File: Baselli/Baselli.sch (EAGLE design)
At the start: 45 parts, among them J2 DF12-ELLI-HEADER-TOP, J3 DF12-ELLI-RECEPTABLE-BOTTOM, J4 FTDI-SER-6-PP, J5 JTAG_PROG, Q1 MOSFET-PCHANNELIRLML2244, U1 LCMXO2-256HC-4SG32, U2 STM32F051R

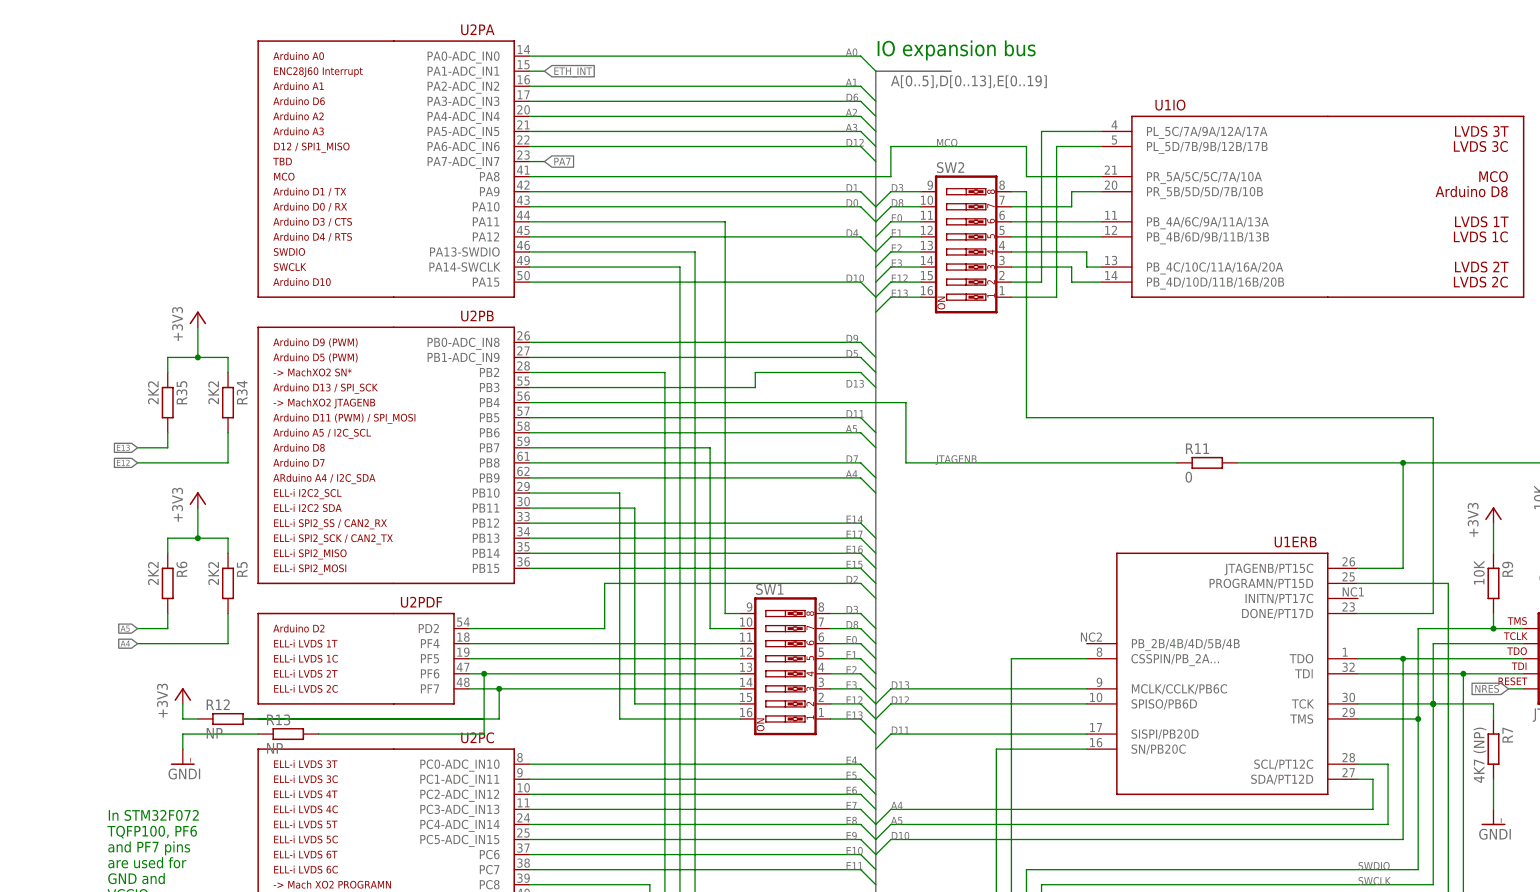
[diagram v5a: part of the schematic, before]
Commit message: Replaced DIP switches with series resistors in Baselli
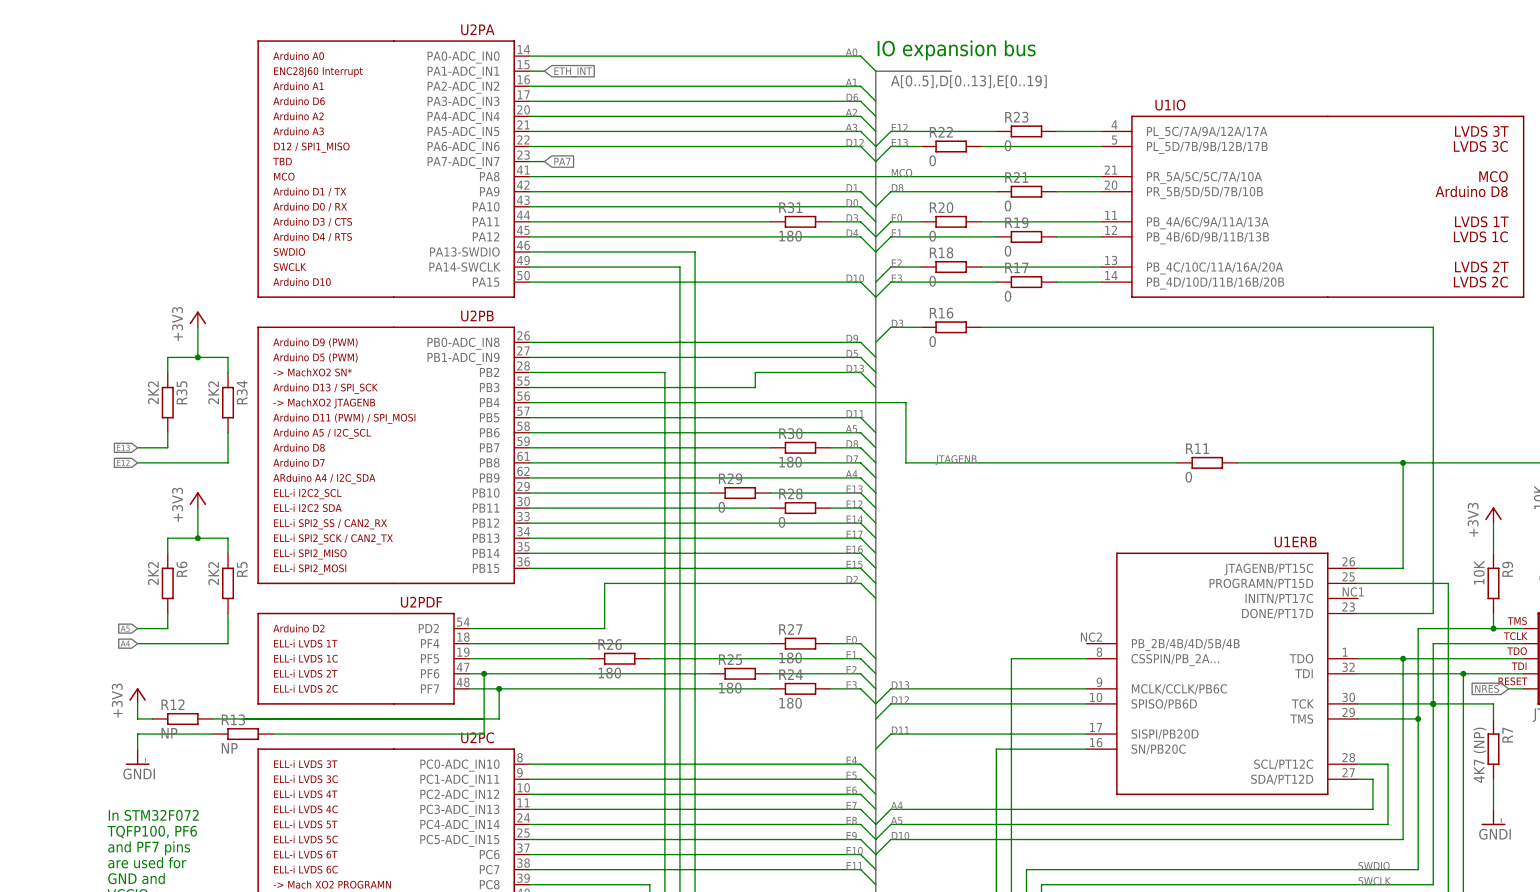
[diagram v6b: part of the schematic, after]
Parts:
- removed SW1, SW2: (no value), SparkFun-Electromechanical:SW_DIP-8-SMT-HALFSIZE
- added R16, R17, R18, R19, R20, R21, R22, R23, R28, R29: 0, ELL-i-Passives:R0805
- added R24, R25, R26, R27, R30, R31: 180, ELL-i-Passives:R0805
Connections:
- net D3: now also R16.1, R31.2; no longer SW1.8, SW2.9
- net D8: now also R21.1, R30.2; no longer SW1.7, SW2.10
- net DONE: now also R16.2; no longer SW2.8
- net E0: now also R20.1, R27.2; no longer SW1.6, SW2.11
- net E1: now also R19.1, R26.2; no longer SW1.5, SW2.12
- net E12: now also R23.1, R28.2; no longer SW1.2, SW2.15
- net E13: now also R22.1, R29.2; no longer SW1.1, SW2.16
- net E2: now also R18.1, R25.2; no longer SW1.4, SW2.13
- net E3: now also R17.1, R24.2; no longer SW1.3, SW2.14
- net N$10: now also R19.2; no longer SW2.5
- net N$12: now also R21.2; no longer SW2.7
- net N$15: now also R18.2; no longer SW2.4
- net N$16: now also R17.2; no longer SW2.3
- net N$17: now also R23.2; no longer SW2.2
- net N$20: now also R22.2; no longer SW2.1
- net N$9: now also R20.2; no longer SW2.6
- net PA11-D3MCU: now also R31.1; no longer SW1.9
- net PB10: now also R29.1; no longer SW1.16
- net PB11: now also R28.1; no longer SW1.15
- net PB7-D8MCU: now also R30.1; no longer SW1.10
- net PF4: now also R27.1; no longer SW1.11
- net PF5: now also R26.1; no longer SW1.12
- net PF6: now also R25.1; no longer SW1.13
- net PF7: now also R24.1; no longer SW1.14
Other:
- moved on the sheet: R12, R13

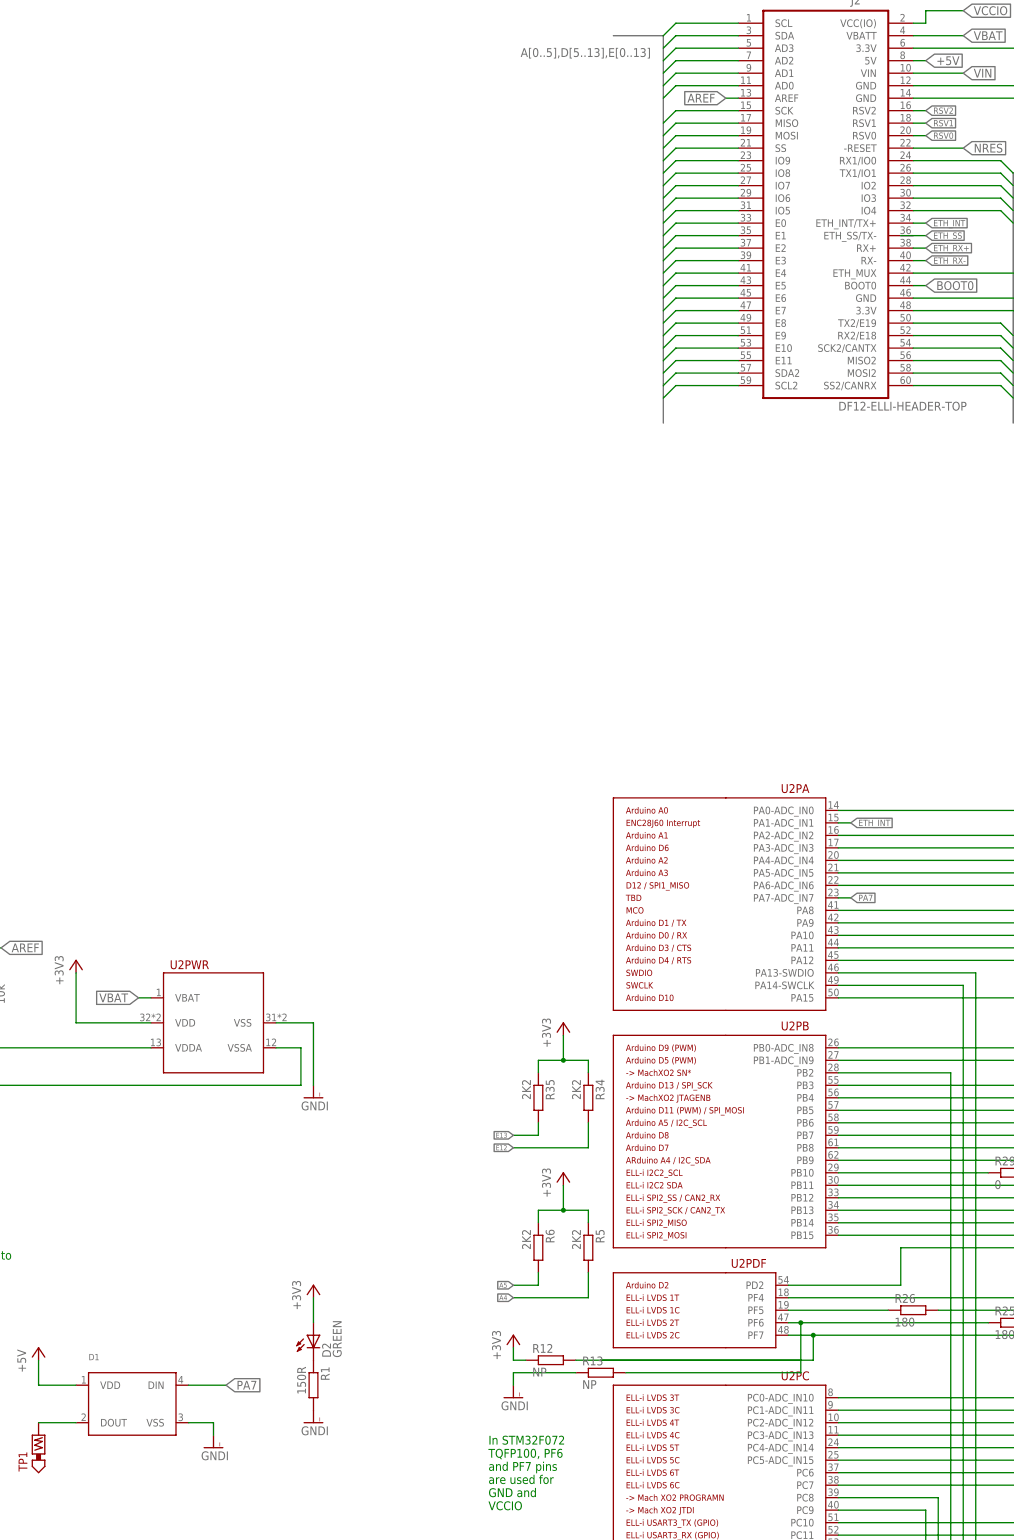
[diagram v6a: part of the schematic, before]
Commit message: Small enhancements to Baselli
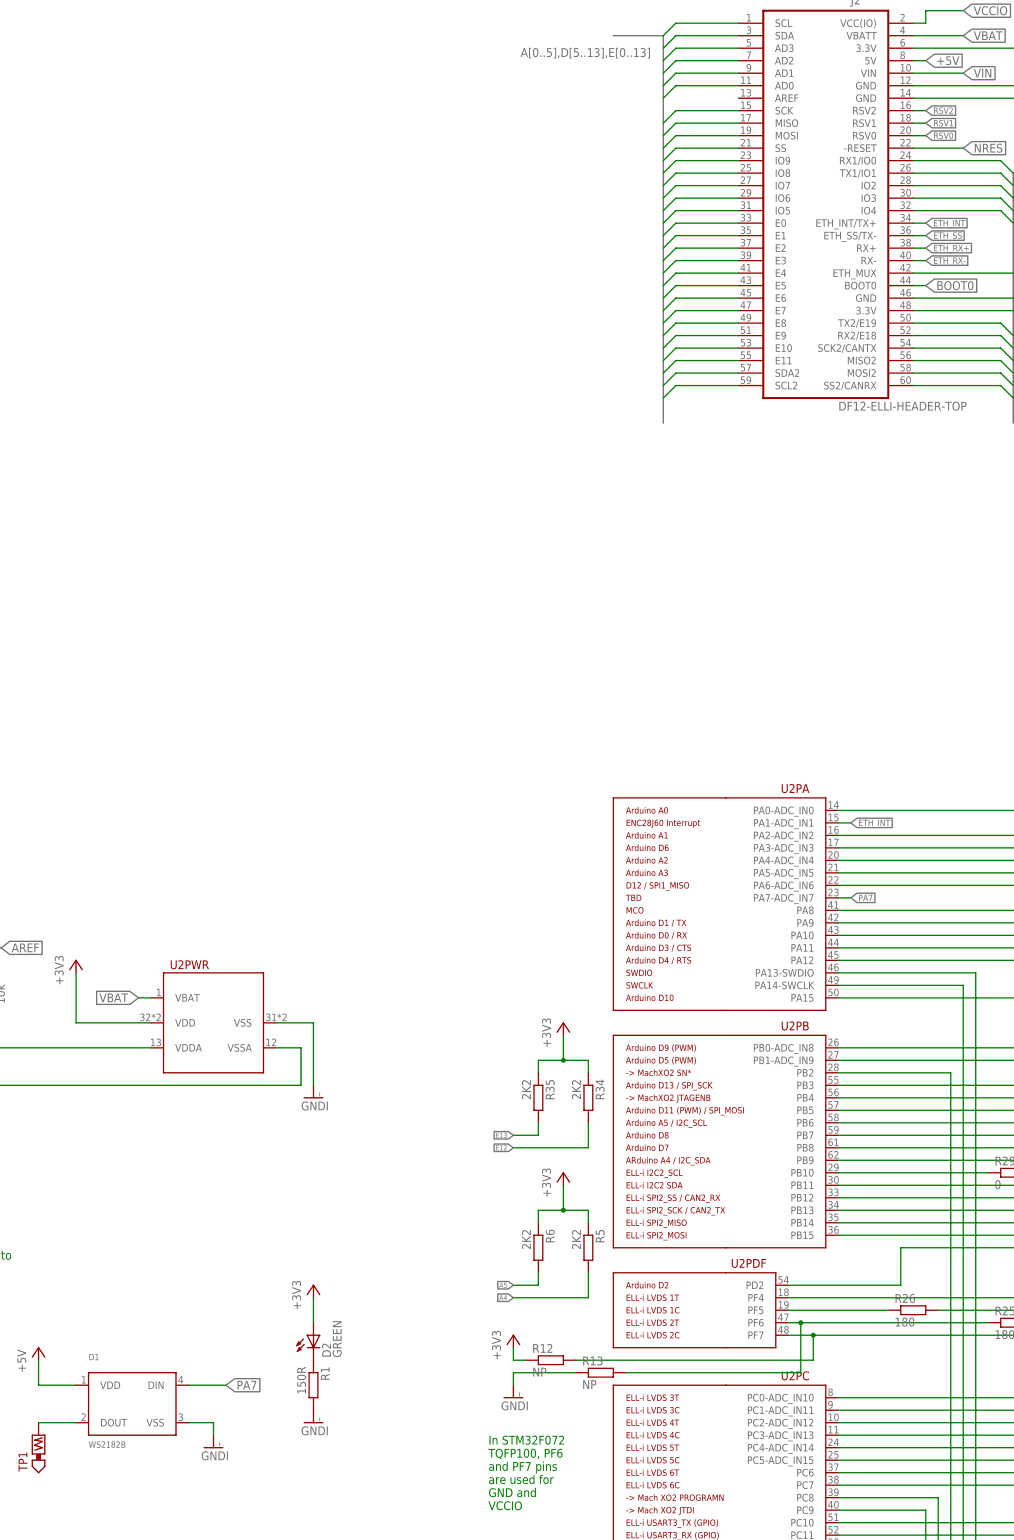
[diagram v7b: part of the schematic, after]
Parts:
- D1: value (none) -> WS2182B
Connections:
- net N$1 renamed JTAGENB$3
- net AREF: no longer J2.AREF
- net ETH_SS: now also J2.ETH_SS/TX-
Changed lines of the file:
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@@
 <part name="R13" library="ELL-i-Passives" deviceset="R" device="0805" value="NP"/>
 <part name="R14" library="ELL-i-Passives" deviceset="R" device="0805" value="NP"/>
-<part name="D1" library="SparkFun-LED" deviceset="WS2812B" device=""/>
+<part name="D1" library="SparkFun-LED" deviceset="WS2812B" device="" value="WS2182B"/>
 <part name="GNDI15" library="supply1" deviceset="GNDI" device=""/>
 <part name="P+2" library="supply1" deviceset="+5V" device=""/>
@@
 <segment>
 <label x="91.44" y="289.56" size="1.27" layer="95" xref="yes"/>
-<wire x1="91.44" y1="289.56" x2="86.36" y2="289.56" width="0.1524" layer="91"/>
+<wire x1="91.44" y1="289.56" x2="88.9" y2="289.56" width="0.1524" layer="91"/>
+<pinref part="J2" gate="E" pin="ETH_SS/TX-"/>
 </segment>
 <segment>
@@
 </segment>
 </net>
-<net name="N$1" class="0">
+<net name="JTAGENB$3" class="0">
 <segment>
 <pinref part="J5" gate="A" pin="3"/>
@@
 <wire x1="114.3" y1="66.04" x2="68.58" y2="66.04" width="0.1524" layer="91"/>
 <pinref part="U2" gate="PDF" pin="PF7"/>
-<pinref part="R12" gate="G$1" pin="2"/>
 <wire x1="68.58" y1="66.04" x2="63.5" y2="66.04" width="0.1524" layer="91"/>
-<wire x1="20.32" y1="60.96" x2="68.58" y2="60.96" width="0.1524" layer="91"/>
 <wire x1="68.58" y1="60.96" x2="68.58" y2="66.04" width="0.1524" layer="91"/>
 <junction x="68.58" y="66.04"/>
 <pinref part="R24" gate="G$1" pin="1"/>
-</segment>
-<segment>
-<wire x1="25.4" y1="60.96" x2="66.04" y2="60.96" width="0.1524" layer="91"/>
+<pinref part="R12" gate="G$1" pin="2"/>
+<wire x1="68.58" y1="60.96" x2="20.32" y2="60.96" width="0.1524" layer="91"/>
 </segment>
 </net>
@@
 <net name="AREF" class="0">
 <segment>
-<pinref part="J2" gate="E" pin="AREF"/>
-<wire x1="53.34" y1="317.5" x2="50.8" y2="317.5" width="0.1524" layer="91"/>
-<label x="50.8" y="317.5" size="1.778" layer="95" rot="R180" xref="yes"/>
-</segment>
-<segment>
 <pinref part="R15" gate="G$1" pin="2"/>

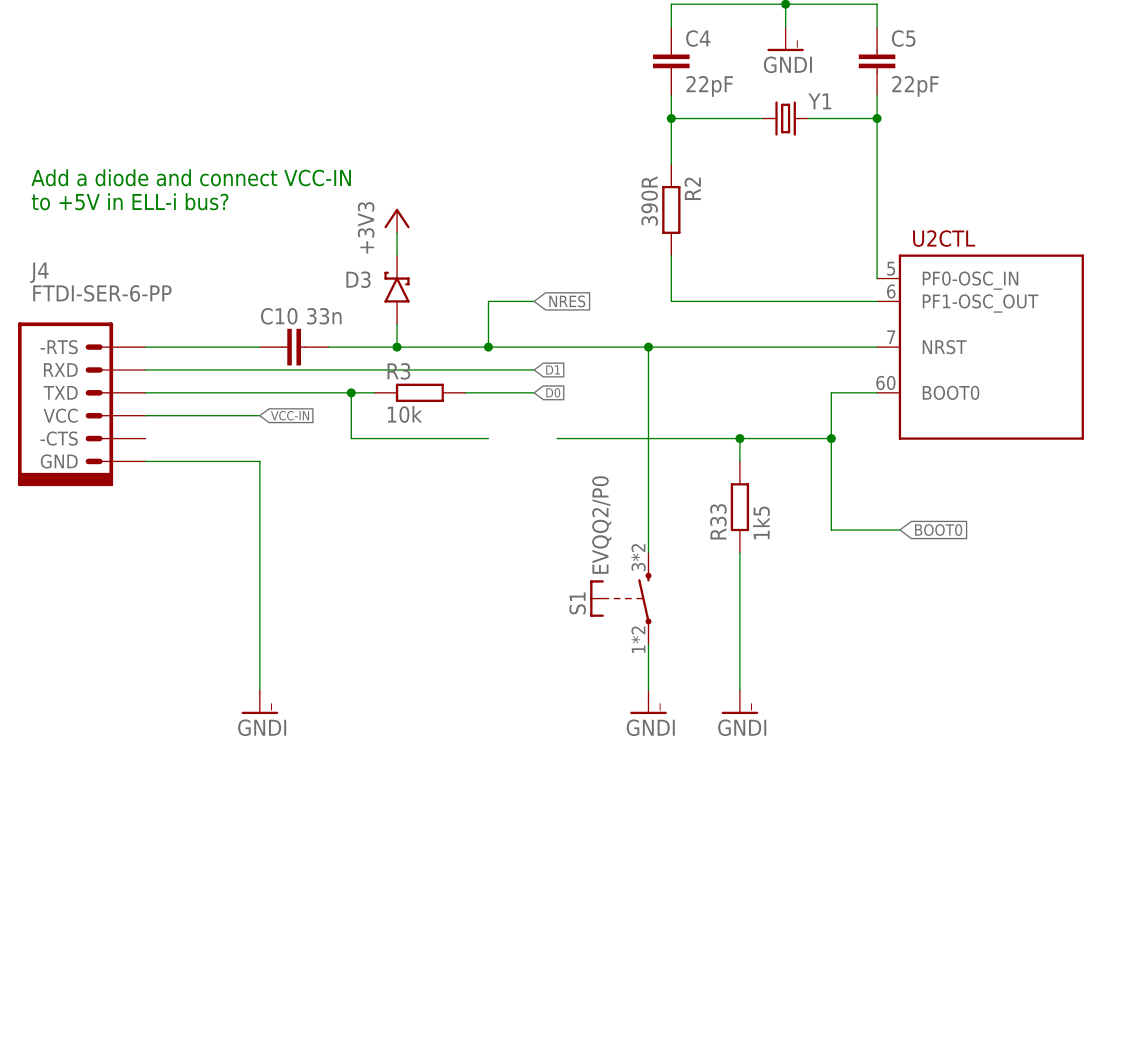
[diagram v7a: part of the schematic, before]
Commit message: Add dip switch & clean up serial programming circuit in Baselli
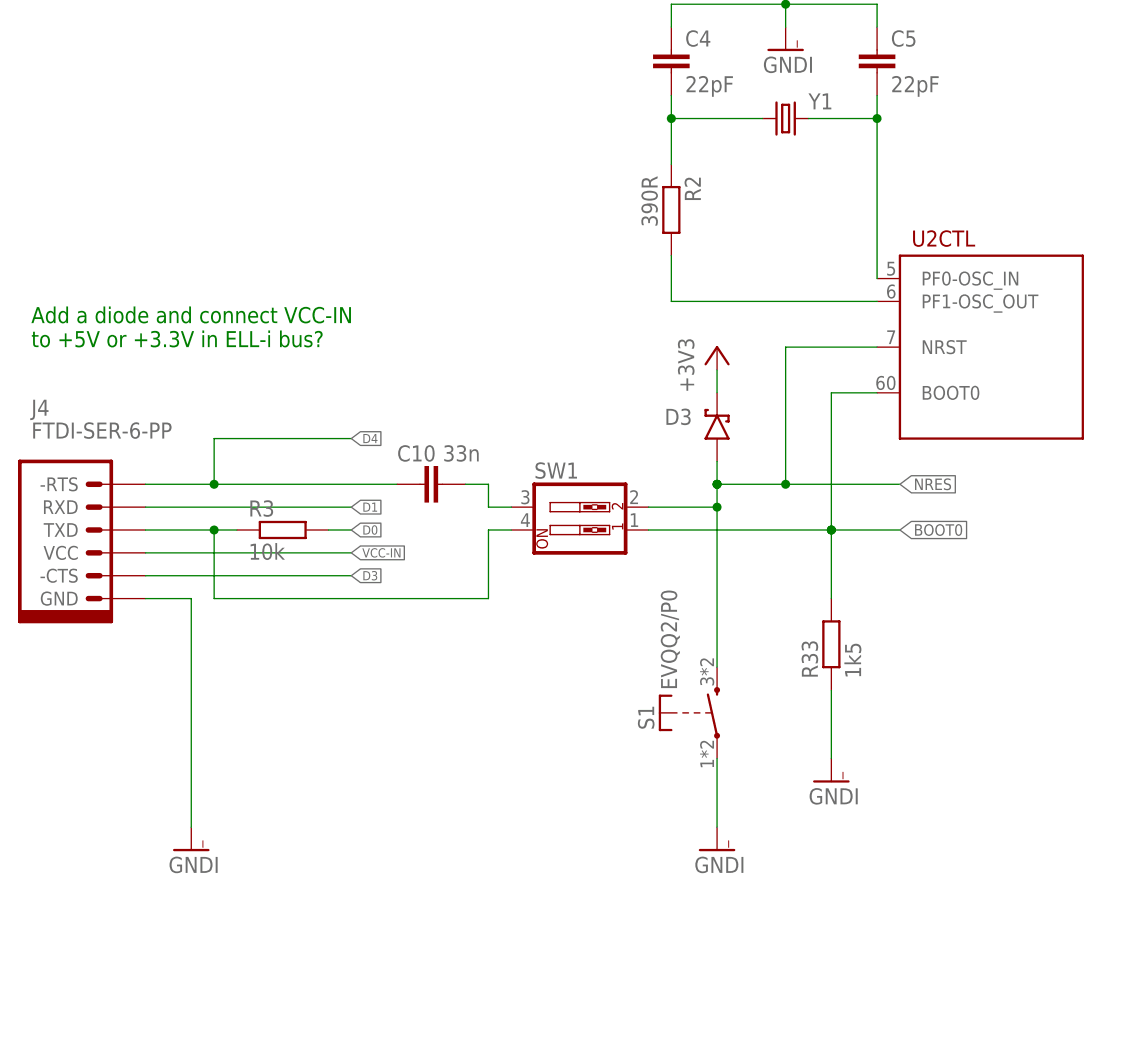
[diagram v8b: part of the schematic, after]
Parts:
- added SW1: (no value), SparkFun-Electromechanical:SW_DIP-2-SMT-HALFSIZE
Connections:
- removed net NDSR1: C10.1, J4.-RTS
- new net -RTS: C10.2, SW1.3
- net BOOT0: now also SW1.1
- net BOOT0TX: now also SW1.4
- net D3: now also J4.-CTS
- net D4: now also C10.1, J4.-RTS
- net NRES: now also SW1.2; no longer C10.2
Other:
- note added: "Add a diode and connect VCC-IN to +5V or +3.3V in ELL-i bus?"
- note removed: "Add a diode and connect VCC-IN to +5V in ELL-i bus?"
- moved on the sheet: C10, D3, J4, R3, R33, S1
